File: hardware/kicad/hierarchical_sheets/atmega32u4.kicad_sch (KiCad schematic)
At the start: 33 parts, among them J1 0475900001, J3 TC2030, U1 ATmega32U4-A, Y2 16MHz

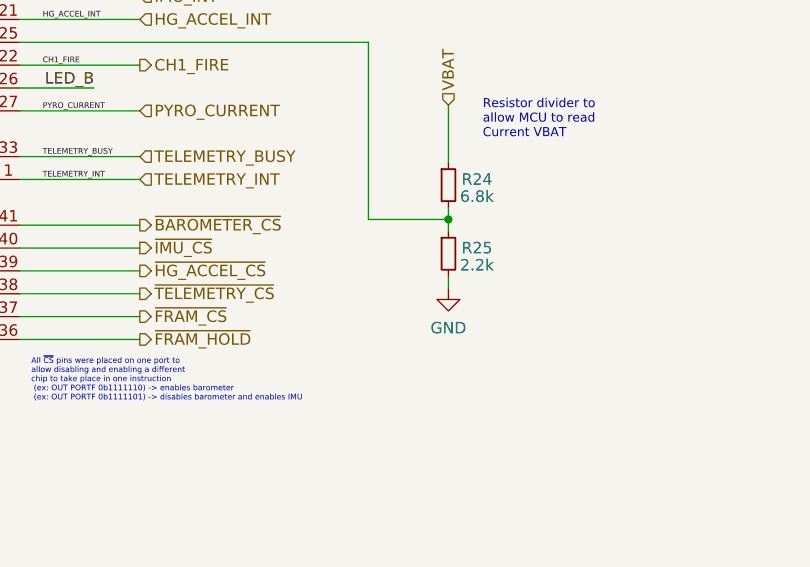
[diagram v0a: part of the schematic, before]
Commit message: added cap to stabilize vbat measurement
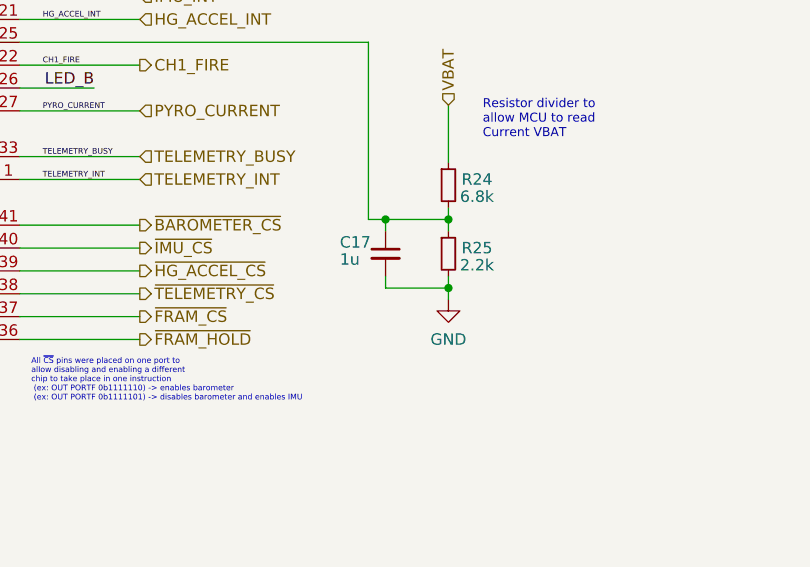
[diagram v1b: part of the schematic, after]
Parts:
- added C17: 1u, symbol Device:C_Small
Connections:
- net GND: now also C17.2
- net at R24.2, R25.1, U1.25 (PD4): now also C17.1
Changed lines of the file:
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@@
   (junction (at 177.8 79.375) (diameter 0) (color 0 0 0 0)
   )
+  (junction (at 153.035 118.11) (diameter 0) (color 0 0 0 0)
+  )
   (junction (at 160.02 118.11) (diameter 0) (color 0 0 0 0)
   )
@@
   )
   (junction (at 95.885 143.51) (diameter 0) (color 0 0 0 0)
+  )
+  (junction (at 160.02 125.73) (diameter 0) (color 0 0 0 0)
   )
   (junction (at 177.8 90.805) (diameter 0) (color 0 0 0 0)
@@
     (stroke (width 0) (type default))
   )
-  (wire (pts (xy 151.13 118.11) (xy 160.02 118.11))
+  (wire (pts (xy 153.035 124.46) (xy 153.035 125.73))
+    (stroke (width 0) (type default))
+  )
+  (wire (pts (xy 151.13 118.11) (xy 153.035 118.11))
+    (stroke (width 0) (type default))
+  )
+  (wire (pts (xy 153.035 118.11) (xy 153.035 119.38))
     (stroke (width 0) (type default))
   )
@@
     (stroke (width 0) (type default))
   )
+  (wire (pts (xy 153.035 118.11) (xy 160.02 118.11))
+    (stroke (width 0) (type default))
+  )
+  (wire (pts (xy 153.035 125.73) (xy 160.02 125.73))
+    (stroke (width 0) (type default))
+  )
   (wire (pts (xy 106.68 32.385) (xy 106.68 34.29))
     (stroke (width 0) (type default))
@@
   )
   (wire (pts (xy 227.33 40.64) (xy 227.33 41.275))
+    (stroke (width 0) (type default))
+  )
+  (wire (pts (xy 160.02 125.73) (xy 160.02 127))
     (stroke (width 0) (type default))
   )
@@
     )
   )
-  (symbol (lib_id "power:GND") (at 160.02 125.73 0) (unit 1)
-    (in_bom yes) (on_board yes) (dnp no)
-    (property "Reference" "#PWR032" (at 160.02 132.08 0)
-      (effects (font (size 1.27 1.27)) hide)
-    )
-    (property "Value" "GND" (at 160.02 130.175 0)
-      (effects (font (size 1.27 1.27)))
-    )
-    (property "Footprint" "" (at 160.02 125.73 0)
-      (effects (font (size 1.27 1.27)) hide)
-    )
-    (property "Datasheet" "" (at 160.02 125.73 0)
+  (symbol (lib_id "power:GND") (at 160.02 127 0) (unit 1)
+    (in_bom yes) (on_board yes) (dnp no)
+    (property "Reference" "#PWR032" (at 160.02 133.35 0)
+      (effects (font (size 1.27 1.27)) hide)
+    )
+    (property "Value" "GND" (at 160.02 131.445 0)
+      (effects (font (size 1.27 1.27)))
+    )
+    (property "Footprint" "" (at 160.02 127 0)
+      (effects (font (size 1.27 1.27)) hide)
+    )
+    (property "Datasheet" "" (at 160.02 127 0)
       (effects (font (size 1.27 1.27)) hide)
     )
@@
         )
       )
+    )
+  )
+  (symbol (lib_id "Device:C_Small") (at 153.035 121.92 0) (unit 1)
+    (in_bom yes) (on_board yes) (dnp no)
+    (property "Reference" "C17" (at 147.955 120.65 0)
+      (effects (font (size 1.27 1.27)) (justify left))
+    )
+    (property "Value" "1u" (at 147.955 122.555 0)
+      (effects (font (size 1.27 1.27)) (justify left))
+    )
+    (property "Footprint" "" (at 153.035 121.92 0)
+      (effects (font (size 1.27 1.27)) hide)
+    )
+    (property "Datasheet" "~" (at 153.035 121.92 0)
+      (effects (font (size 1.27 1.27)) hide)
+    )
+    (pin "1")
+    (pin "2")
+    (instances
+      (project "FC"
+        (path "/54cce219-8b98-4e71-96c4-f9ee784aa3bc/aac89dea-c005-40db-a234-32c8ed41f1e5"
+          (reference "C17") (unit 1)
+        )
+      )

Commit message: added power and checked schematics
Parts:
- added F1: Fuse, symbol Device:Fuse
- added TP10, TP11, TP6, TP9: TestPoint, TestPoint:TestPoint_Pad_D1.5mm, symbol Connector:TestPoint
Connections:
- net BUZZER_PWM: now also TP11.1
- net LED_B: now also TP10.1
- net LED_G: now also TP9.1
- net LED_R: now also TP6.1
- net USB_CONN_D+: no longer J1.3 (D+)
- net USB_CONN_D-: no longer J1.2 (D-)
- net VBUS: now also F1.2; no longer J1.1 (VBUS)
- new net: F1.1, J1.1 (VBUS)
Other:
- note added: "TEST POINTS"
- note removed: "GROUND STATION CONVERSION"
- note removed: "TODO: Add disconnect jumpers for certain pins"
- moved on the sheet: J1

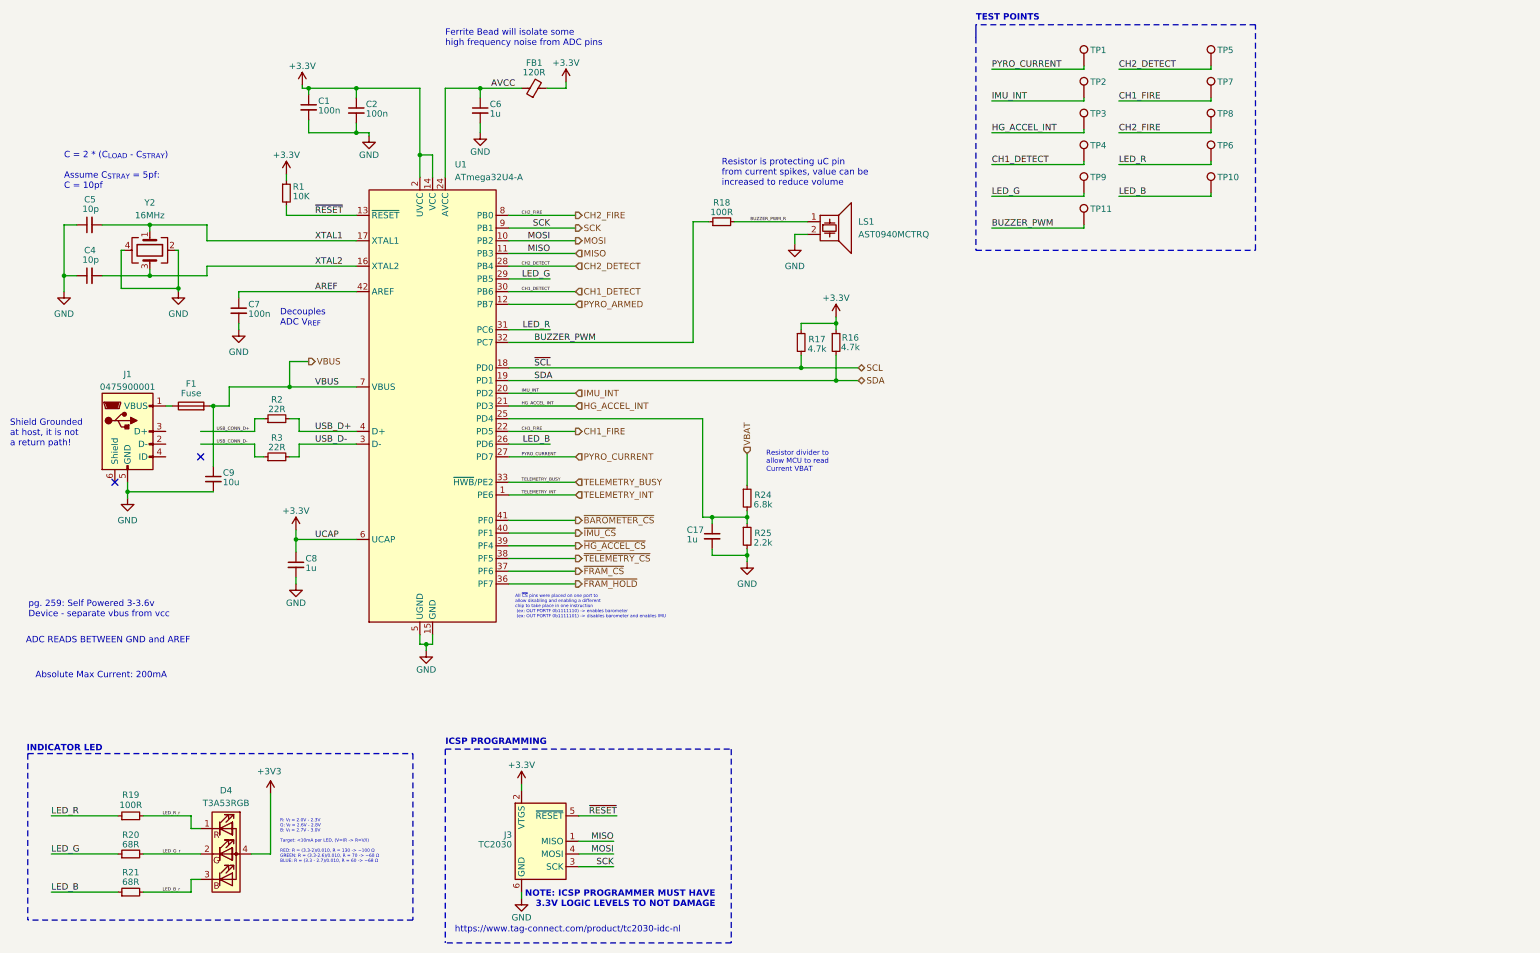
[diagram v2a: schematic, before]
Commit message: assigned footprints
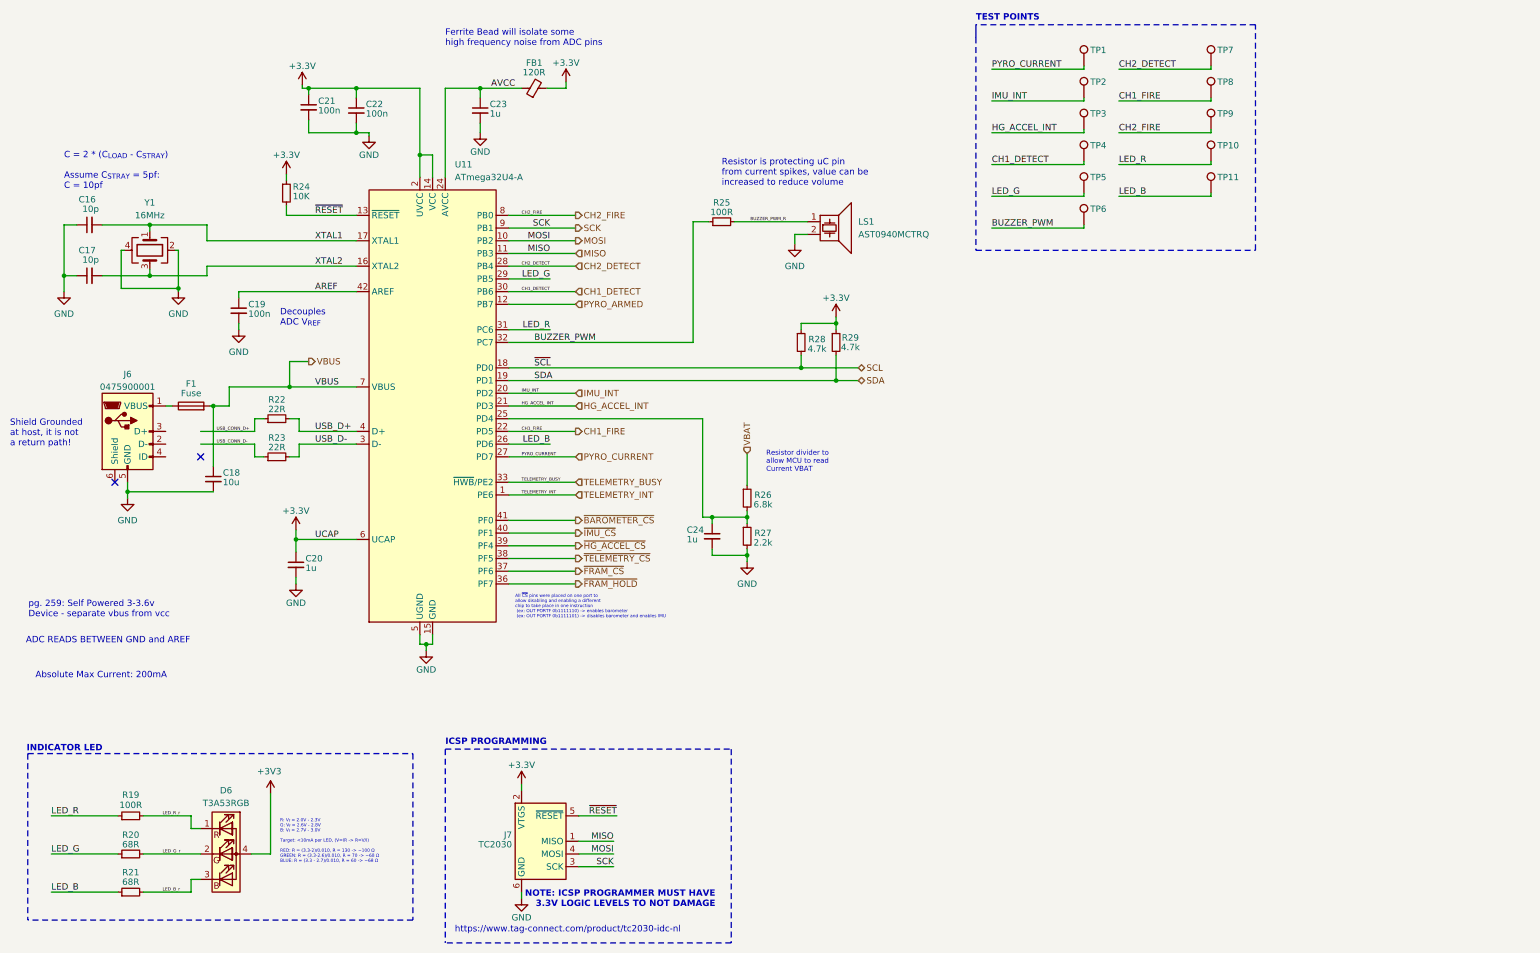
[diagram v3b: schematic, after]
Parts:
- C16: renamed from C5; footprint (none) -> Resistor_SMD:R_0603_1608Metric
- C17: renamed from C4; footprint (none) -> Resistor_SMD:R_0603_1608Metric
- C18: renamed from C9; footprint (none) -> Resistor_SMD:R_0603_1608Metric
- C19: renamed from C7; footprint (none) -> Resistor_SMD:R_0603_1608Metric
- C20: renamed from C8; footprint (none) -> Resistor_SMD:R_0603_1608Metric
- C21: renamed from C1; footprint (none) -> Resistor_SMD:R_0603_1608Metric
- C22: renamed from C2; footprint (none) -> Resistor_SMD:R_0603_1608Metric
- C23: renamed from C6; footprint (none) -> Resistor_SMD:R_0603_1608Metric
- C24: renamed from C17; footprint (none) -> Resistor_SMD:R_0603_1608Metric
- F1, R19, R20, R21: footprint (none) -> Resistor_SMD:R_0603_1608Metric
- R22: renamed from R2; footprint (none) -> Resistor_SMD:R_0603_1608Metric
- R23: renamed from R3; footprint (none) -> Resistor_SMD:R_0603_1608Metric
- R24: renamed from R1; footprint (none) -> Resistor_SMD:R_0603_1608Metric
- R25: renamed from R18; footprint (none) -> Resistor_SMD:R_0603_1608Metric
- R26: renamed from R24; footprint (none) -> Resistor_SMD:R_0603_1608Metric
- R27: renamed from R25; footprint (none) -> Resistor_SMD:R_0603_1608Metric
- R28: renamed from R17; footprint (none) -> Resistor_SMD:R_0603_1608Metric
- R29: renamed from R16; footprint (none) -> Resistor_SMD:R_0603_1608Metric
- renumbered D4 to D6, J1 to J6, J3 to J7, TP6 to TP10, TP10 to TP11, TP9 to TP5, TP11 to TP6, TP5 to TP7, TP7 to TP8, TP8 to TP9, U1 to U11, Y2 to Y1

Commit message: making formatting more consistent
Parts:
- F1: value Fuse -> 500mA
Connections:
- net VBAT_SENSE: now reaches C24.1, R26.2, R27.1, U11.25 (PD4)
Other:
- note removed: "ADC READS BETWEEN GND and AREF"
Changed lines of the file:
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@@
     (effects (font (size 0.63 0.63)) (justify left bottom))
-  )
-  (text "ADC READS BETWEEN GND and AREF" (at 15.875 143.51 0)
-    (effects (font (size 1.27 1.27)) (justify left bottom))
   )
   (text "https://www.tag-connect.com/product/tc2030-idc-nl" (at 101.6 201.295 0)
@@
   )
   (text "pg. 259: Self Powered 3-3.6v \nDevice - separate vbus from vcc"
-    (at 16.383 138.303 0)
+    (at 27.94 125.095 0)
     (effects (font (size 1.27 1.27)) (justify left bottom))
   )
@@
   (label "LED_B" (at 120.65 103.505 180) (fields_autoplaced)
     (effects (font (size 1.27 1.27)) (justify right bottom))
+  )
+  (label "VBAT_SENSE" (at 114.935 98.425 0) (fields_autoplaced)
+    (effects (font (size 0.63 0.63)) (justify left bottom))
   )
   (label "CH2_DETECT" (at 114.935 67.945 0) (fields_autoplaced)
@@
   (symbol (lib_id "Device:C_Small") (at 153.035 121.92 0) (unit 1)
     (in_bom yes) (on_board yes) (dnp no)
-    (property "Reference" "C24" (at 147.955 120.65 0)
-      (effects (font (size 1.27 1.27)) (justify left))
-    )
-    (property "Value" "1u" (at 147.955 122.555 0)
+    (property "Reference" "C24" (at 147.32 120.65 0)
+      (effects (font (size 1.27 1.27)) (justify left))
+    )
+    (property "Value" "1u" (at 147.32 122.555 0)
       (effects (font (size 1.27 1.27)) (justify left))
     )
@@
       (effects (font (size 1.27 1.27)))
     )
-    (property "Value" "Fuse" (at 48.895 93.345 90)
-      (effects (font (size 1.27 1.27)))
-    )
+    (property "Value" "500mA" (at 48.895 93.345 90)
+      (effects (font (size 1.27 1.27)))
+    )
